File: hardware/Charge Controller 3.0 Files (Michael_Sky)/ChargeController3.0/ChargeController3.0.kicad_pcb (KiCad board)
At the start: 2 copper layers, 95.9 x 90.2 mm, 85 parts, among them J1 Conn_02x26_Odd_Even, J10 SOL_TEST_01x01_Pin, J11 GND_TEST_01x01_Pin, J12 Conn_02x26_Odd_Even, J17 SCL_MAS_01x01_Pin, J18 SDA_MAS_01x01_Pin, J19 SYS-1x2, J2 SP_01x02_Pin, J20 Conn_01x08_Pin, J3 BATT_TEST_01x01_Pin, J4 3.3V_PULLUP_01x02_Pin, J5 BATT_01x02_Pin, J9 SYS_TEST_01x01_Pin, Q1 SI2318CDS-T1-GE3, Q10 SI2318CDS-T1-GE3, Q11 SI2318CDS-T1-GE3, Q2 SI2318CDS-T1-GE3, Q3 SI2318CDS-T1-GE3, Q4 SI2318CDS-T1-GE3, Q5 AONS66614, Q6 AONS66614, Q7 AONS66614, Q8 AONS66614, Q9 SI2318CDS-T1-GE3, SW1 100SP1T1B1M1QEH, U1 BQ25756ERRVR

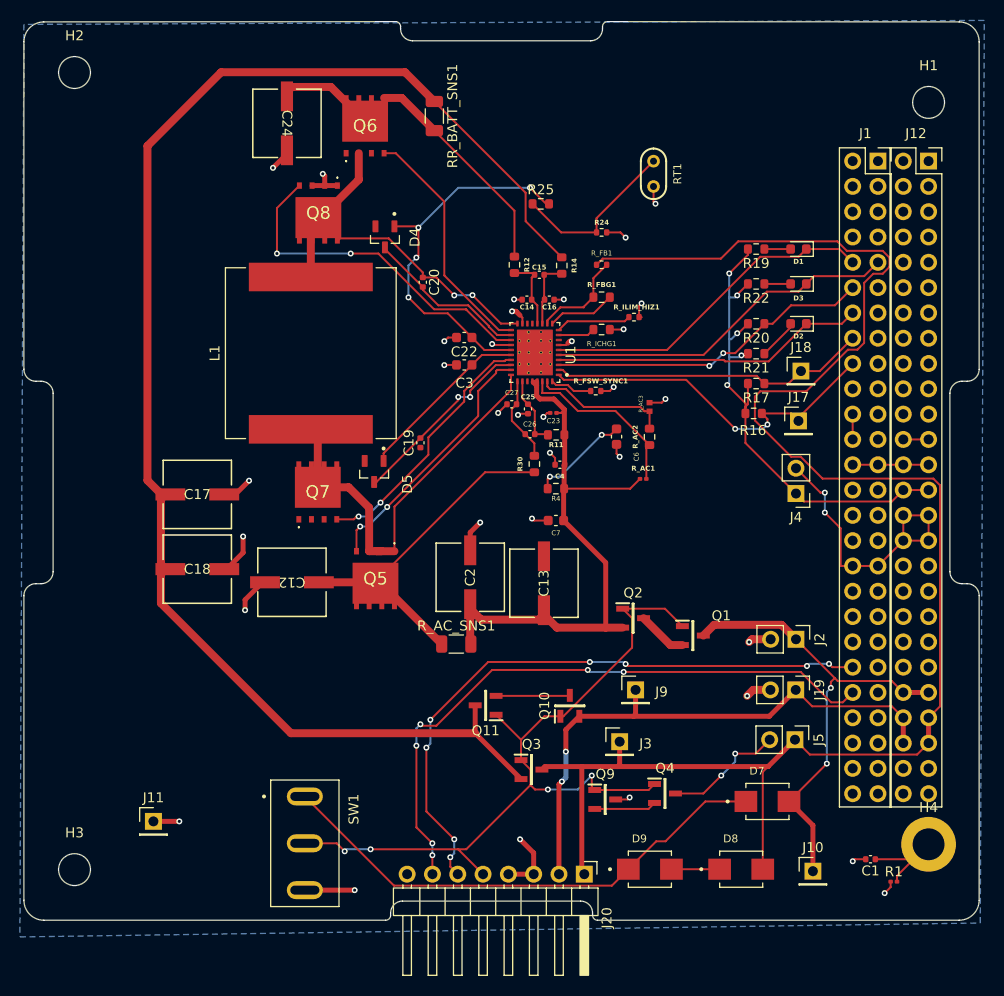
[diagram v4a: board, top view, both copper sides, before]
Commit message: Final PCB?
inhibits rework, filtering rework
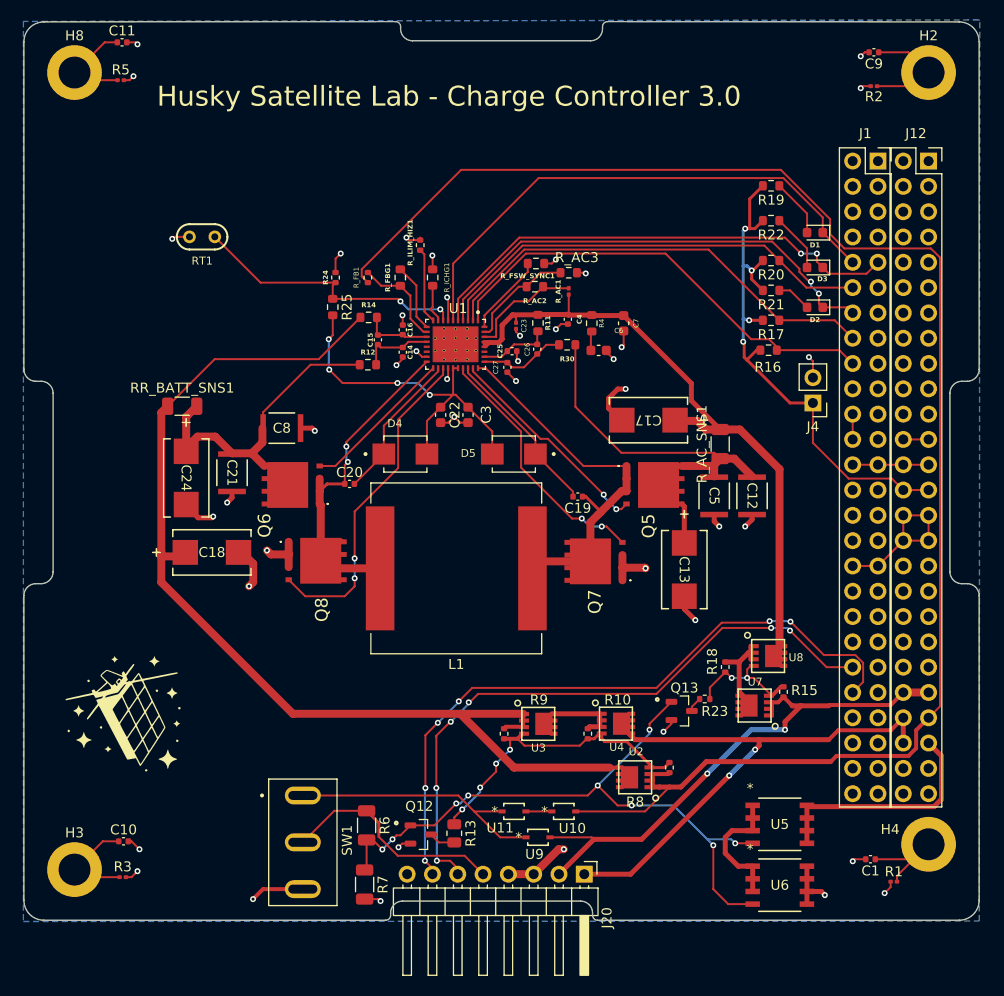
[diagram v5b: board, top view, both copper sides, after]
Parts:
- removed C2: 56u, bmsfootprints:CAP_UCD_6P3X7P7_NCH
- removed D7, D8, D9: SS24, bmsfootprints:SS24
- removed H1: MountingHole, MountingHole:MountingHole_3.2mm_M3_ISO14580
- removed J10: SOL_TEST_01x01_Pin, Connector_PinHeader_2.54mm:PinHeader_1x01_P2.54mm_Vertical
- removed J11: GND_TEST_01x01_Pin, Connector_PinHeader_2.54mm:PinHeader_1x01_P2.54mm_Vertical
- removed J17: SCL_MAS_01x01_Pin, Connector_PinHeader_2.54mm:PinHeader_1x01_P2.54mm_Vertical
- removed J18: SDA_MAS_01x01_Pin, Connector_PinHeader_2.54mm:PinHeader_1x01_P2.54mm_Vertical
- removed J19: SYS-1x2, Connector_PinHeader_2.54mm:PinHeader_1x02_P2.54mm_Vertical
- removed J2: SP_01x02_Pin, Connector_PinHeader_2.54mm:PinHeader_1x02_P2.54mm_Vertical
- removed J3: BATT_TEST_01x01_Pin, Connector_PinHeader_2.54mm:PinHeader_1x01_P2.54mm_Vertical
- removed J5: BATT_01x02_Pin, Connector_PinHeader_2.54mm:PinHeader_1x02_P2.54mm_Vertical
- removed J9: SYS_TEST_01x01_Pin, Connector_PinHeader_2.54mm:PinHeader_1x01_P2.54mm_Vertical
- removed Q1, Q10, Q11, Q2, Q3, Q4, Q9: SI2318CDS-T1-GE3, bmsfootprints:SI2318CDS-T1-GE3
- added C10: 100nF, Capacitor_SMD:C_0402_1005Metric, F.Cu at (114.0, 142.2)
- added C11: 100nF, Capacitor_SMD:C_0402_1005Metric, F.Cu at (113.9, 62.0)
- added C21: 10u, bmsfootprints:CGA6P1X7R1N106K250AC, F.Cu at (124.9, 105.2)
- added C5: 10u, bmsfootprints:CGA6P1X7R1N106K250AC, F.Cu at (173.3, 107.5)
- added C8: 10u, bmsfootprints:CGA6P1X7R1N106K250AC, F.Cu at (129.9, 100.7)
- added C9: 100nF, Capacitor_SMD:C_0402_1005Metric, F.Cu at (189.3, 63.0)
- added G***: LOGO, bmsfootprints:logoHSL, F.Cu at (114.2, 129.4)
- added H8: MountingHole_Pad, MountingHole:MountingHole_3.2mm_M3_ISO14580_Pad, F.Cu at (109.1, 65.0)
- added Q12: SOT91P240X110-3N, bmsfootprints:2N7002K-7, F.Cu at (143.8, 141.5)
- added Q13: SOT91P240X110-3N, bmsfootprints:2N7002K-7, F.Cu at (170.0, 129.1)
- added R10: 1M, Resistor_SMD:R_0402_1005Metric, F.Cu at (160.6, 131.4)
- added R13: 400k, Resistor_SMD:R_0805_2012Metric, F.Cu at (147.2, 141.4)
- added R15: 1M, Resistor_SMD:R_0402_1005Metric, F.Cu at (180.2, 127.2)
- added R18: 1M, Resistor_SMD:R_0402_1005Metric, F.Cu at (174.4, 124.7)
- added R2: 1M, Resistor_SMD:R_0201_0603Metric, F.Cu at (189.3, 66.4)
- added R23: 200k, Resistor_SMD:R_0402_1005Metric, F.Cu at (172.3, 127.9)
- added R3: 1M, Resistor_SMD:R_0201_0603Metric, F.Cu at (113.9, 145.8)
- added R5: 1M, Resistor_SMD:R_0201_0603Metric, F.Cu at (113.7, 65.8)
- added R6: 330k, Resistor_SMD:R_1206_3216Metric, F.Cu at (138.4, 140.6)
- added R7: 470k, Resistor_SMD:R_1206_3216Metric, F.Cu at (138.2, 146.5)
- added R8: 1M, Resistor_SMD:R_0402_1005Metric, F.Cu at (168.8, 134.8)
- added R9: 1M, Resistor_SMD:R_0402_1005Metric, F.Cu at (152.2, 131.4)
- added U10: BAT46WJ_115, bmsfootprints:BAT46WJ115, F.Cu at (158.2, 139.2)
- added U11: BAT46WJ_115, bmsfootprints:BAT46WJ115, F.Cu at (153.2, 139.2)
- added U2: SISH101DN-T1-GE3, bmsfootprints:SISH, F.Cu at (165.7, 135.8)
- added U3: SISH101DN-T1-GE3, bmsfootprints:SISH, F.Cu at (155.3, 130.4)
- added U4: SISH101DN-T1-GE3, bmsfootprints:SISH, F.Cu at (163.1, 130.4)
- added U5: SI4122DY-T1-GE3, bmsfootprints:SI4122., F.Cu at (179.9, 140.5)
- added U6: SI4122DY-T1-GE3, bmsfootprints:SI4122., F.Cu at (179.9, 146.6)
- added U7: SISH101DN-T1-GE3, bmsfootprints:SISH, F.Cu at (177.6, 128.6)
- added U8: SISH101DN-T1-GE3, bmsfootprints:SISH, F.Cu at (178.4, 123.6)
- added U9: BAT46WJ_115, bmsfootprints:BAT46WJ115, F.Cu at (155.6, 141.8)
- C12: value 56u -> 10u; footprint bmsfootprints:CAP_UCD_6P3X7P7_NCH -> bmsfootprints:CGA6P1X7R1N106K250AC
- C13, C17, C18, C24: value 56u -> 100u; footprint bmsfootprints:CAP_UCD_6P3X7P7_NCH -> bmsfootprints:T520D107
- D4, D5: value BAT54 -> DIOM4336X265N; footprint bmsfootprints:BAT54 -> bmsfootprints:SS26
- H2, H3: value MountingHole -> MountingHole_Pad; footprint MountingHole:MountingHole_3.2mm_M3_ISO14580 -> MountingHole:MountingHole_3.2mm_M3_ISO14580_Pad
- R_AC2: value 11.83k -> 40.2k
- R_AC3: value RC0402FR-0753K6L -> 60.4k; footprint bmsfootprints:RC0402FR-0753K6L -> Resistor_SMD:R_0603_1608Metric
- R_FBG1: value 16.67k -> 16.2k
- R_FSW_SYNC1: value 40k -> 133k; footprint Resistor_SMD:R_0402_1005Metric -> Resistor_SMD:R_0603_1608Metric
- moved H2 85.7 mm to (194.8, 65.0)
- moved C12 47.0 mm to (177.1, 107.5), turned to -90 degrees
- moved C17 45.9 mm to (166.7, 99.9), turned to 180 degrees
- moved RT1 45.7 mm to (121.9, 81.5), turned to 180 degrees
- moved RR_BATT_SNS1 38.6 mm to (119.9, 98.5), turned to 0 degrees
- moved C24 37.0 mm to (120.3, 105.7)
- moved Q6 36.8 mm to (130.9, 106.4), turned to 90 degrees
- moved Q8 34.9 mm to (133.3, 114.0), turned to -90 degrees
- moved R_AC_SNS1 33.2 mm to (173.9, 102.3), turned to 90 degrees
- moved Q5 29.5 mm to (167.2, 106.4), turned to -90 degrees
- moved Q7 28.7 mm to (161.3, 114.1), turned to 90 degrees
- moved R24 27.1 mm to (135.3, 85.6), turned to -90 degrees
- moved L1 26.1 mm to (147.4, 114.8), turned to 180 degrees
- moved R_FB1 23.5 mm to (138.5, 85.6), turned to 90 degrees
- moved R25 23.3 mm to (135.0, 88.6), turned to -90 degrees
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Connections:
- C13 pad 1: IN -> Net-(Q5-D_1)
- C17 pad 1: OUT -> IN
- J12 pad 45: BATT_PIN -> BATT+_PIN
- J12 pad 47: BATT_PIN -> BATT-_PIN
- J20 pad 1: BATT_PIN -> SYS_PIN
- J20 pad 2: SYS_PIN -> SOL_PIN
- R_FB1 pad 1: BATT_PIN -> BATT+_PIN
- U1 pad 38: (no net) -> GND
- U1 pad 39: (no net) -> GND
- U1 pad 40: (no net) -> GND
- U1 pad 41: (no net) -> GND
- U1 pad 42: (no net) -> GND
- U1 pad 43: (no net) -> GND
- U1 pad 44: (no net) -> GND
- U1 pad 45: (no net) -> GND
- U1 pad 46: (no net) -> GND
- U1 pad 47: (no net) -> GND
- U1 pad 48: (no net) -> GND
- U1 pad 49: (no net) -> GND
- U1 pad 50: (no net) -> GND
- U1 pad 51: (no net) -> GND
- U1 pad 52: (no net) -> GND
- U1 pad 53: (no net) -> GND
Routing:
- net BATT_PIN: track 169.6 -> 0.00 mm
- net BATT+_PIN: track 0.00 -> 160.1 mm
- net DIV: track 0.00 -> 68.6 mm, vias 0 -> 9
- net EN: track 78.5 -> 22.8 mm, vias 4 -> 0
- net OUT: track 149.2 -> 106.7 mm
- net Net-(U2-G): track 0.00 -> 30.7 mm, vias 0 -> 4
- net Net-(SW1-Pad1): track 51.5 -> 26.9 mm
- net BATT-_PIN: track 0.00 -> 23.8 mm
- net PG: track 34.2 -> 53.8 mm
- net DRV_SUP: track 55.4 -> 37.1 mm
- net STAT_1: track 31.6 -> 47.6 mm, vias 0 -> 2
- net SDA: track 32.0 -> 45.9 mm
- net STAT_2: track 35.9 -> 49.3 mm, vias 0 -> 2
- net Net-(U5-Pad1): track 0.00 -> 13.0 mm
- net Net-(J5-Pin_2): track 12.2 -> 0.00 mm, vias 2 -> 0
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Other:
- board text added: "Husky Satellite Lab - Charge Controller 3.0"
